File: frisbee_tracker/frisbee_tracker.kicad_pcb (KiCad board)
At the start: 2 copper layers, 38.1 x 38.1 mm, 63 parts, among them IC1 NRF54L05-QFAA-R7, J1 UJC-H-G-SMT-2-P6-TR, J2 FTSH-105-01-L-DV-K, U1 AP2210N-3.3TRG1, U2 BQ24072RGTT, U3 BMI323, U4 BSS138, U5 BSS138, U6 BSS138, U7 BSS138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

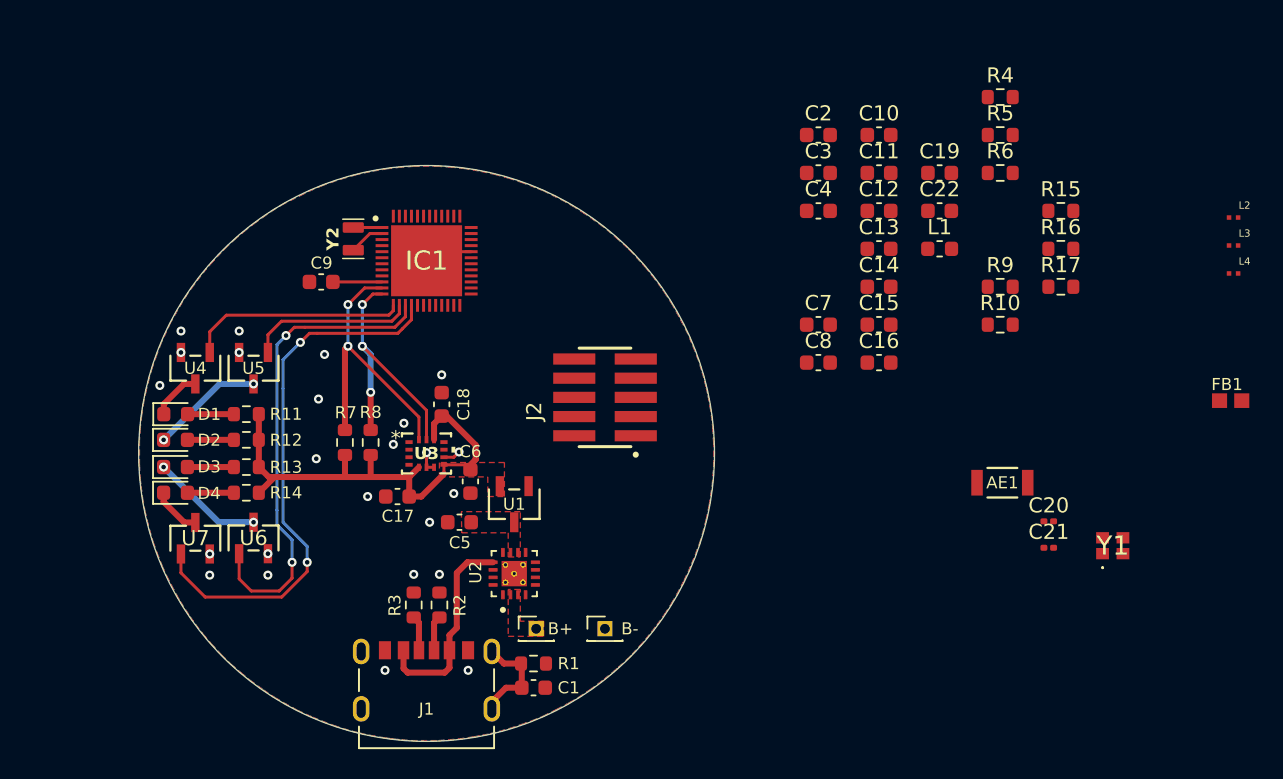
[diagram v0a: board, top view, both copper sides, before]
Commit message: PCB design 75 percent complete
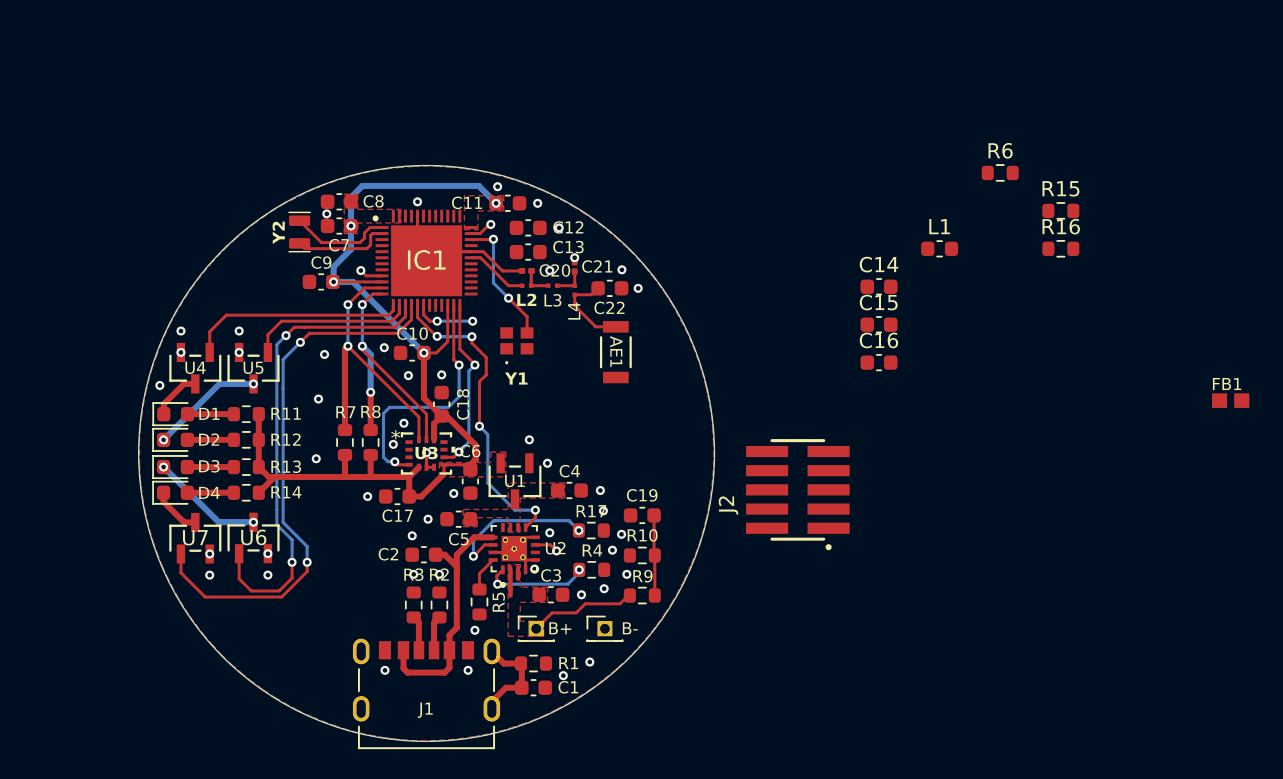
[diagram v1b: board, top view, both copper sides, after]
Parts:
- Y1: value 32 MHz -> ECS-320-8-37B2-JTY-TR
- moved L2 47.0 mm to (156.4, 88.5)
- moved R5 46.3 mm to (153.3, 109.5), turned to -90 degrees
- moved L3 45.1 mm to (158.2, 88.5)
- moved L4 43.6 mm to (159.6, 88.8), turned to -90 degrees
- moved Y1 41.7 mm to (155.8, 92.2)
- moved R4 41.3 mm to (160.7, 107.3)
- moved C20 38.3 mm to (156.4, 87.6)
- moved C2 38.1 mm to (149.6, 106.3), turned to 180 degrees
- moved C21 36.5 mm to (159.6, 87.3), turned to 90 degrees
- moved R17 35.0 mm to (160.7, 104.8), turned to 180 degrees
- moved C10 34.1 mm to (148.8, 93.0)
- moved C8 33.4 mm to (144.0, 83.0)
- moved C3 33.0 mm to (158.0, 109.0)
- moved C7 32.4 mm to (144.0, 84.6)
- moved R9 31.3 mm to (164.1, 109.0), turned to 180 degrees
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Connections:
- Y1 pad 2: Net-(IC1-XC1) -> GND
- Y1 pad 3: (no net) -> Net-(IC1-XC1)
- Y1 pad 4: (no net) -> GND
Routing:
- net Net-(IC1-VDD_1): track 35.6 -> 68.9 mm, vias 0 -> 4
- net Net-(IC1-P2.06/TRACECLK/SPI.SCK): track 0.00 -> 20.7 mm, vias 0 -> 4
- net Net-(IC1-P0.00): track 0.00 -> 16.4 mm, vias 0 -> 2
- net GND: track 4.67 -> 17.3 mm, vias 23 -> 49
- net Net-(IC1-P0.01): track 1.14 -> 11.8 mm, vias 1 -> 2
- net Net-(U2-TMR): track 0.00 -> 10.4 mm, vias 0 -> 2
- net Net-(U2-BAT): track 0.00 -> 9.41 mm
- net Net-(IC1-XC1): track 0.00 -> 8.61 mm, vias 0 -> 2
- net Net-(U2-TS): track 0.00 -> 7.05 mm, vias 0 -> 2
- net Net-(IC1-P1.08/CLK16M/TAMPC): track 0.00 -> 7.04 mm, vias 0 -> 1
- net Net-(AE1-Pad1): track 0.00 -> 5.76 mm
- net Net-(IC1-P2.07/TRACEDATA[0]/SWO/SPI.DCX): track 0.00 -> 5.62 mm, vias 0 -> 3
- net Net-(IC1-P1.00/XL1): track 1.90 -> 6.66 mm
- net Net-(IC1-ANT): track 0.00 -> 4.14 mm
- net Net-(IC1-P1.01/XL2): track 2.36 -> 6.38 mm
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
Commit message: rework on controller PCB wiring started
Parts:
- moved FB1 72.5 mm to (131.9, 81.7), turned to -90 degrees
- moved L1 50.2 mm to (134.1, 79.0), turned to 180 degrees
- moved C14 45.6 mm to (134.7, 81.7), turned to 180 degrees
- moved C15 33.2 mm to (149.7, 76.9)
- moved C10 25.0 mm to (125.0, 85.6)
- moved AE1 18.3 mm to (173.4, 78.4)
- moved Y1 15.3 mm to (163.7, 79.1)
- moved C1 14.9 mm to (142.1, 113.0), turned to 0 degrees
- moved R1 14.8 mm to (142.1, 114.6), turned to 0 degrees
- moved C21 14.1 mm to (173.7, 86.5)
- moved L4 14.1 mm to (173.7, 88.0)
- moved C20 14.1 mm to (170.5, 86.8)
- moved C22 14.1 mm to (176.0, 87.9)
- moved L2 14.1 mm to (170.5, 87.8)
- moved L3 14.1 mm to (172.2, 87.8)
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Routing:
- net Net-(IC1-VDD_1): track 68.9 -> 37.0 mm, vias 4 -> 0
- net Net-(IC1-P2.06/TRACECLK/SPI.SCK): track 20.7 -> 9.29 mm, vias 4 -> 2
- net GND: track 17.3 -> 7.04 mm, vias 49 -> 41
- net Net-(IC1-XC1): track 8.61 -> 0.00 mm, vias 2 -> 0
- net Net-(IC1-P2.05/SPI.CS): track 36.2 -> 28.2 mm
- net Net-(IC1-P2.04/SPI.SDI/SDO): track 31.7 -> 24.7 mm
- net Net-(IC1-P1.00/XL1): track 6.66 -> 0.00 mm
- net Net-(IC1-P1.01/XL2): track 6.38 -> 0.00 mm
- net Net-(AE1-Pad1): track 5.76 -> 0.00 mm
- net Net-(IC1-P0.01): track 11.8 -> 7.33 mm, vias 2 -> 1
- net Net-(IC1-ANT): track 4.14 -> 0.00 mm
- net Net-(IC1-P0.00): track 16.4 -> 12.4 mm, vias 2 -> 1
- net Net-(IC1-P2.07/TRACEDATA[0]/SWO/SPI.DCX): track 5.62 -> 1.57 mm, vias 3 -> 1
- net Net-(C20-Pad2): track 2.08 -> 0.00 mm
- net Net-(C21-Pad1): track 2.08 -> 0.00 mm
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
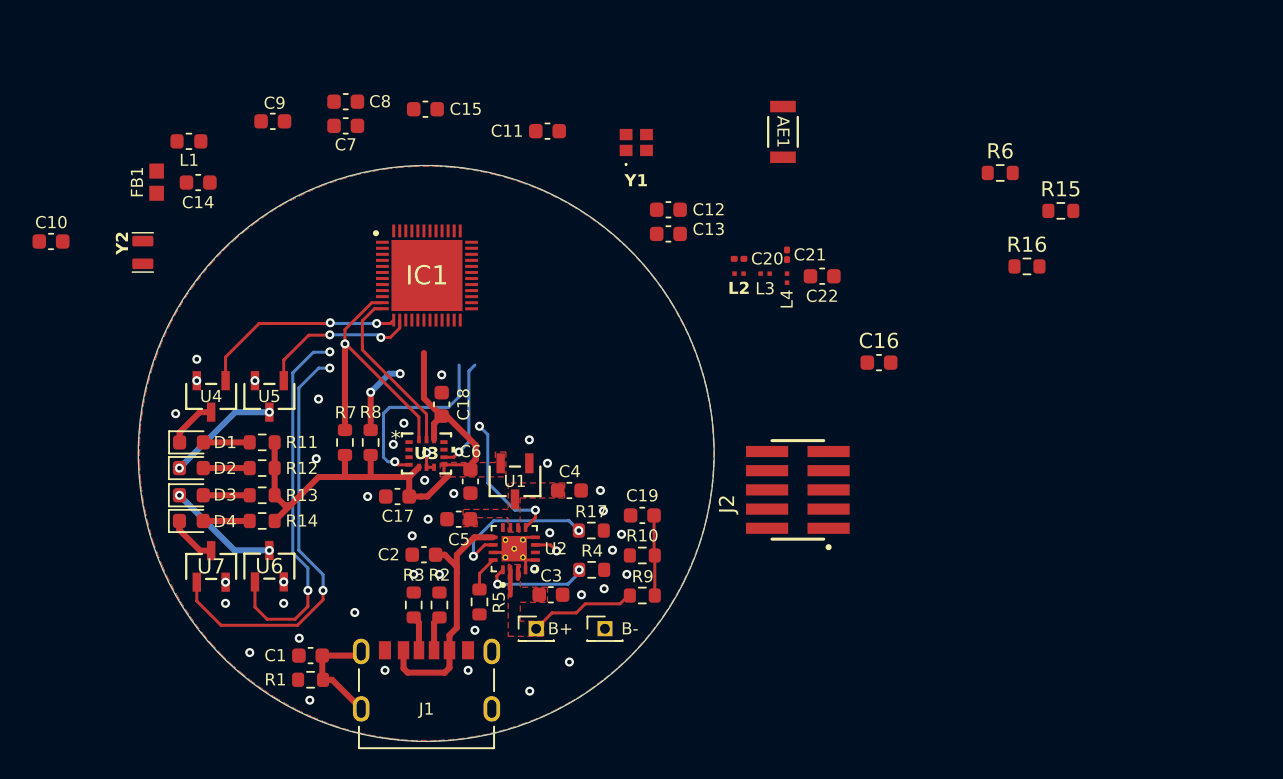
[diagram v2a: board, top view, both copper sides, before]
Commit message: PCB rework of MCU
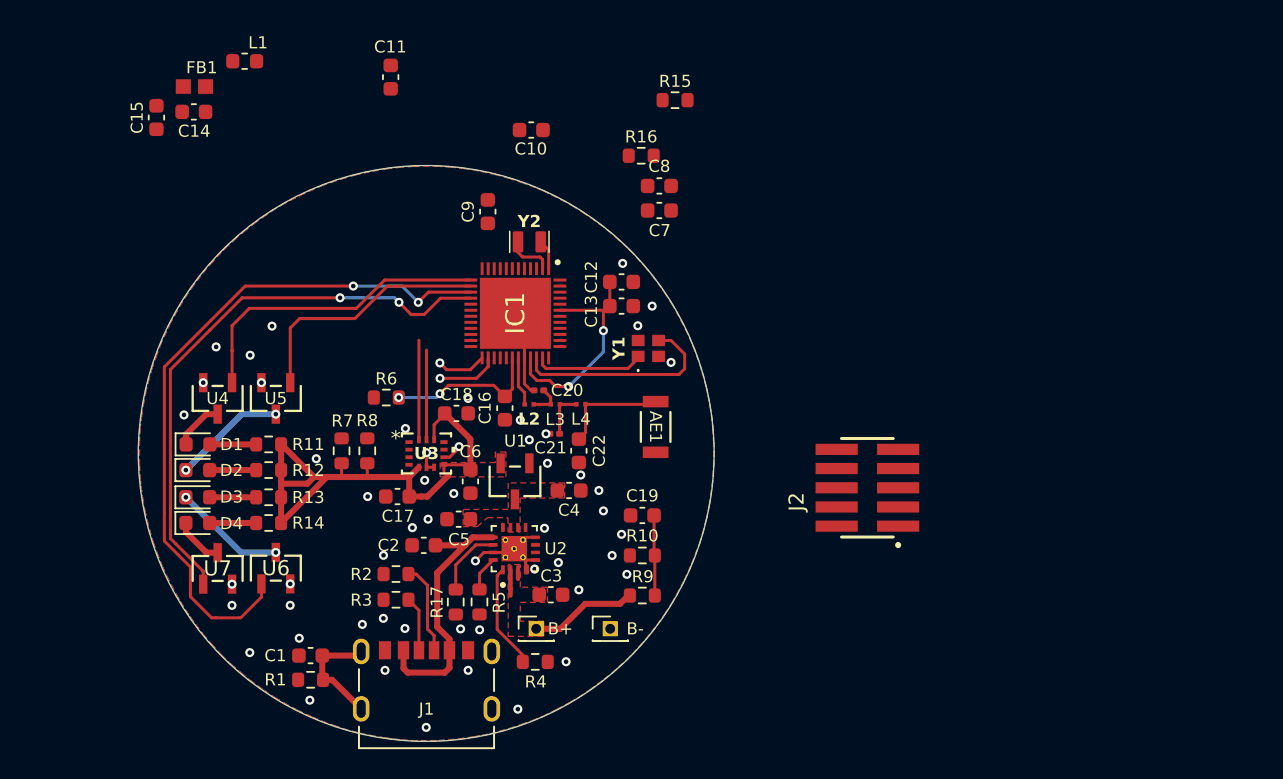
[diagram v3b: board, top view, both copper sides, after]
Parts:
- moved R6 43.3 mm to (147.1, 96.0), turned to 180 degrees
- moved C10 32.6 mm to (156.7, 78.2), turned to 180 degrees
- moved R16 26.6 mm to (164.0, 80.0)
- moved R15 26.6 mm to (166.2, 76.3)
- moved Y2 25.6 mm to (156.6, 85.7), turned to 0 degrees
- moved C16 24.9 mm to (155.0, 96.7), turned to 90 degrees
- moved C7 21.5 mm to (165.2, 83.6)
- moved C8 21.5 mm to (165.2, 82.0)
- moved AE1 21.3 mm to (165.0, 97.9)
- moved C22 19.8 mm to (159.9, 99.5), turned to 90 degrees
- moved C21 19.4 mm to (158.3, 98.3), turned to 180 degrees
- moved C15 17.8 mm to (131.9, 77.4), turned to 90 degrees
- moved L2 16.4 mm to (156.6, 96.4)
- moved L3 16.4 mm to (158.3, 96.4)
- moved L4 16.0 mm to (160.0, 96.4), turned to 0 degrees
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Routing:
- net Net-(IC1-P2.04/SPI.SDI/SDO): track 24.7 -> 45.8 mm
- net Net-(IC1-DECA): track 0.00 -> 15.4 mm, vias 0 -> 2
- net Net-(IC1-XC1): track 0.00 -> 14.0 mm
- net Net-(IC1-P0.00): track 12.4 -> 0.00 mm, vias 1 -> 0
- net Net-(IC1-P2.00/SPI.DCX): track 18.0 -> 6.58 mm, vias 1 -> 0
- net Net-(IC1-NRESET): track 0.00 -> 10.6 mm, vias 0 -> 2
- net Net-(IC1-P2.01/SPI.SCK): track 16.2 -> 5.93 mm, vias 2 -> 0
- net Net-(IC1-P2.05/SPI.CS): track 28.2 -> 37.8 mm
- net Net-(IC1-P2.06/TRACECLK/SPI.SCK): track 9.29 -> 0.00 mm, vias 2 -> 0
- net GND: track 7.04 -> 14.9 mm, vias 41 -> 52
- net Net-(IC1-XC2): track 0.00 -> 7.30 mm
- net Net-(AE1-Pad1): track 0.00 -> 7.26 mm
- net Net-(IC1-P2.02/SPI.SDI/SDO): track 13.7 -> 20.8 mm, vias 2 -> 0
- net Net-(IC1-P2.03): track 10.6 -> 16.7 mm, vias 2 -> 0
- net Net-(IC1-P0.01): track 7.33 -> 1.33 mm
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
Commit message: PCB design 90% complete
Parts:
- J2: value FTSH-105-01-L-DV-K -> FTSH-103-01-L-D; footprint footprints:FTSH-105-01-L-DV-K -> footprints:FTSH-103-01-L-D
- Y1: value ECS-320-8-37B2-JTY-TR -> 32 MHz
- moved J2 40.5 mm to (141.9, 85.6), turned to 0 degrees
- moved R15 25.4 mm to (144.8, 89.9), turned to 180 degrees
- moved R16 22.4 mm to (144.8, 91.5), turned to 180 degrees
- moved C11 21.2 mm to (159.6, 92.1)
- moved L1 20.9 mm to (156.2, 83.6)
- moved C15 20.5 mm to (151.2, 84.3)
- moved C14 20.4 mm to (153.8, 83.2), turned to 90 degrees
- moved C10 19.2 mm to (147.4, 95.0), turned to 90 degrees
- moved FB1 18.1 mm to (151.3, 82.0)
- moved C16 15.5 mm to (147.8, 82.9), turned to -90 degrees
- moved C13 12.3 mm to (152.7, 97.1), turned to 90 degrees
- moved C12 12.2 mm to (154.3, 97.1), turned to 90 degrees
- moved R6 10.2 mm to (146.3, 85.8), turned to 90 degrees
- moved C8 6.83 mm to (162.7, 88.3), turned to 180 degrees
- moved C7 6.55 mm to (163.6, 89.9), turned to 180 degrees
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- renumbered B+ to H1, B- to H2
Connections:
- J2 pad 01: (no net) -> Net-(IC1-VDD_1)
- J2 pad 02: (no net) -> Net-(IC1-SWDIO)
- J2 pad 03: (no net) -> GND
- J2 pad 04: (no net) -> Net-(IC1-SWDCLK)
- J2 pad 05: (no net) -> GND
- J2 pad 06: (no net) -> Net-(J2-Pad06)
- R6 pad 2: Net-(J2-Pad6) -> Net-(J2-Pad06)
- U2 pad 18: GND -> (no net)
- U2 pad 19: GND -> (no net)
- U2 pad 20: GND -> (no net)
- U2 pad 21: GND -> (no net)
- U2 pad 22: GND -> (no net)
- U2 pad 7: Net-(IC1-P2.07/TRACEDATA[0]/SWO/SPI.DCX) -> Net-(IC1-P2.06/TRACECLK/SPI.SCK)
- U2 pad 9: Net-(IC1-P2.06/TRACECLK/SPI.SCK) -> Net-(IC1-P2.07/TRACEDATA[0]/SWO/SPI.DCX)
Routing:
- net Net-(IC1-VDD_1): track 37.4 -> 87.3 mm, vias 0 -> 10
- net Net-(IC1-P1.08/CLK16M/TAMPC): track 5.50 -> 50.1 mm, vias 0 -> 2
- net Net-(IC1-P2.06/TRACECLK/SPI.SCK): track 0.00 -> 38.3 mm, vias 0 -> 2
- net Net-(IC1-P2.07/TRACEDATA[0]/SWO/SPI.DCX): track 0.00 -> 33.9 mm, vias 0 -> 2
- net Net-(IC1-DECA): track 15.4 -> 37.8 mm, vias 2 -> 4
- net Net-(IC1-DECD): track 0.00 -> 14.7 mm, vias 0 -> 2
- net Net-(IC1-P2.00/SPI.DCX): track 6.58 -> 20.3 mm, vias 0 -> 2
- net Net-(IC1-P2.01/SPI.SCK): track 5.93 -> 19.5 mm, vias 0 -> 3
- net Net-(IC1-P0.00): track 0.00 -> 13.3 mm, vias 0 -> 2
- net Net-(IC1-P0.01): track 1.33 -> 10.4 mm, vias 1 -> 2
- net Net-(IC1-DCC): track 0.00 -> 8.44 mm
- net GND: track 14.9 -> 22.2 mm, vias 52 -> 73
- net Net-(IC1-NRESET): track 10.6 -> 5.06 mm
- net Net-(IC1-SWDCLK): track 4.25 -> 1.66 mm
- net Net-(J2-Pad06): track 0.00 -> 2.07 mm
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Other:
- board text added: "ALAN BOVEE JAKE WAUN"
- board text added: "GND"
- board text added: "SWCLK"
- board text added: "SWDIO"
- board text added: "VCC"
- board text added: "WayWayWay"
- board text added: "nRESET"

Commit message: Rough draft of PCB completed
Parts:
- J1: value UJC-H-G-SMT-2-P6-TR -> SAMESKY_UJC-H-G-SMT-2-P6-TR
- moved R7 0.48 mm to (144.8, 93.6)
- moved R8 0.48 mm to (144.8, 95.2)
- renumbered H1 to B+, H2 to B-
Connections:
- J1 pad SH3: Net-(J1-SHIELD) -> (no net)
- J1 pad SH4: Net-(J1-SHIELD) -> (no net)
- U2 pad 18: (no net) -> GND
- U2 pad 19: (no net) -> GND
- U2 pad 20: (no net) -> GND
- U2 pad 21: (no net) -> GND
- U2 pad 22: (no net) -> GND
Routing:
- net Net-(IC1-SWDIO): track 1.42 -> 22.8 mm
- net Net-(IC1-SWDCLK): track 1.66 -> 22.2 mm
- net Net-(IC1-NRESET): track 5.06 -> 21.0 mm
- net Net-(IC1-P0.01): track 10.4 -> 8.89 mm, vias 2 -> 0
- net Net-(IC1-XC1): track 14.5 -> 13.2 mm
- net Net-(J1-SHIELD): track 8.43 -> 7.56 mm
- net Net-(U1-VIN): track 0.00 -> 0.83 mm
- net Net-(IC1-VDD_1): track 87.3 -> 88.1 mm, vias 10 -> 9
- net Net-(IC1-DECA): track 37.8 -> 37.2 mm
- net Net-(IC1-P1.08/CLK16M/TAMPC): track 50.1 -> 50.2 mm, vias 2 -> 4
- net Net-(J2-Pad06): vias 0 -> 1
- net GND: vias 73 -> 90

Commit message: Added switch and Shottky diode to schematic
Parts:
- added D5: SMD26PL-TP, footprints:SMD26PL-TP, F.Cu at (148.8, 107.2)
- added H3: Switch In, Connector_PinHeader_1.27mm:PinHeader_1x01_P1.27mm_Vertical, F.Cu at (175.8, 101.4)
- added H4: Switch Out, Connector_PinHeader_1.27mm:PinHeader_1x01_P1.27mm_Vertical, F.Cu at (175.8, 104.8)
- J1: value SAMESKY_UJC-H-G-SMT-2-P6-TR -> UJC-H-G-SMT-2-P6-TR
- moved R2 2.65 mm to (145.1, 107.6)
- moved R3 2.65 mm to (145.1, 109.3)
- moved U1 0.59 mm to (155.7, 100.9)
- renumbered B+ to H1, B- to H2
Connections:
- C4 pad 1: Net-(U1-VIN) -> Net-(U2-OUT)
- C5 pad 2: Net-(U1-VIN) -> Net-(D5-K)
- IC1 pad 50: GND -> (no net)
- J1 pad SH3: (no net) -> unconnected-(J1-SHIELD__2-PadSH3)
- J1 pad SH4: (no net) -> unconnected-(J1-SHIELD__3-PadSH4)
- U1 pad 3: Net-(U1-VIN) -> Net-(D5-K)
- U2 pad 10: Net-(U1-VIN) -> Net-(U2-OUT)
- U2 pad 11: Net-(U1-VIN) -> Net-(U2-OUT)
- U2 pad 18: GND -> (no net)
- U2 pad 19: GND -> (no net)
- U2 pad 20: GND -> (no net)
- U2 pad 21: GND -> (no net)
- U2 pad 22: GND -> (no net)
- Y1 pad 2: GND -> Net-(IC1-XC1)
- Y1 pad 3: Net-(IC1-XC1) -> (no net)
- Y1 pad 4: GND -> (no net)
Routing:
- net GND: track 22.2 -> 27.6 mm, vias 90 -> 94
- net Net-(J1-CC1): track 3.63 -> 5.06 mm
- net Net-(U1-VIN): track 0.83 -> 0.00 mm
- net Net-(J1-CC2): track 6.05 -> 6.84 mm
- removed copper zone on F.Cu, net Net-(U1-VIN)

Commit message: PCB design complete and Gerbers generated
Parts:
- moved SW 15.0 mm to (160.8, 102.7)
- moved SW 9.68 mm to (166.3, 102.7)
- moved R3 1.88 mm to (143.6, 108.2), turned to 90 degrees
- moved C4 1.49 mm to (158.3, 101.4), turned to 90 degrees
- moved C2 1.49 mm to (149.4, 107.2), turned to -90 degrees
- moved D5 1.40 mm to (147.4, 107.1)
- moved R2 0.61 mm to (145.3, 108.2), turned to 90 degrees
- moved C5 0.55 mm to (152.0, 103.5)
- moved C6 0.38 mm to (152.7, 101.1)
- moved U1 0.08 mm to (155.6, 100.9)
- renumbered H1 to B+, H2 to B-, H4 to SW, H3 to SW
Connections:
- IC1 pad 50: (no net) -> GND
- U2 pad 18: (no net) -> GND
- U2 pad 19: (no net) -> GND
- U2 pad 20: (no net) -> GND
- U2 pad 21: (no net) -> GND
- U2 pad 22: (no net) -> GND
- Y1 pad 2: Net-(IC1-XC1) -> GND
- Y1 pad 3: (no net) -> Net-(IC1-XC1)
- Y1 pad 4: (no net) -> GND
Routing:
- net Net-(D5-K): track 0.00 -> 21.2 mm, vias 0 -> 2
- net Net-(U2-OUT): track 0.00 -> 6.09 mm
- net Net-(D5-A): track 17.7 -> 22.0 mm
- net Net-(J1-CC1): track 5.06 -> 7.90 mm
- net GND: track 27.6 -> 27.9 mm, vias 94 -> 100
- added copper zone on F.Cu, net Net-(U2-OUT)
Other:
- board text added: "BOVEE WAUN"
- board text removed: "ALAN BOVEE JAKE WAUN"
